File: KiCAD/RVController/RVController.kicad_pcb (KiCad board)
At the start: 2 copper layers, 1 part, among them U1 FREESOC_MINI

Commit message: Getting started
Added GaN NFET output channels, started work on input channels
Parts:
- added C1: 10UF, Capacitor_SMD:C_1206_3216Metric, F.Cu at (114.3, 71.1)
- added J1: 1727078, Footprints:PHOENIX_1727078, F.Cu at (73.7, 66.0)
- added J2: 1727078, Footprints:PHOENIX_1727078, F.Cu at (40.0, 124.5)
- added J3: 1727078, Footprints:PHOENIX_1727078, F.Cu at (40.6, 66.0)
- added J4: 1727078, Footprints:PHOENIX_1727078, F.Cu at (73.7, 124.5)
- added Q1: EPC2014C, Footprints:TRANS_EPC2014C, F.Cu at (92.5, 91.1)
- added Q2: EPC2014C, Footprints:TRANS_EPC2014C, F.Cu at (88.7, 91.1)
- added Q3: EPC2014C, Footprints:TRANS_EPC2014C, F.Cu at (88.7, 88.5)
- added Q4: EPC2014C, Footprints:TRANS_EPC2014C, F.Cu at (92.5, 88.5)
- added Q5: EPC2014C, Footprints:TRANS_EPC2014C, F.Cu at (84.9, 88.5)
- added Q6: EPC2014C, Footprints:TRANS_EPC2014C, F.Cu at (81.0, 91.1)
- added Q7: EPC2014C, Footprints:TRANS_EPC2014C, F.Cu at (76.2, 78.7)
- added Q8: EPC2014C, Footprints:TRANS_EPC2014C, F.Cu at (84.9, 91.1)
- added U2: 74HCT541, Package_DIP:DIP-20_W7.62mm_LongPads, F.Cu at (82.6, 100.3)
- moved U1 62.7 mm to (26.7, 109.2), turned to 90 degrees
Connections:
- U1 pad 20: unconnected-(U1-Pad20) -> GND
- U1 pad 21: unconnected-(U1-Pad21) -> XPWM1
- U1 pad 22: unconnected-(U1-Pad22) -> XPWM2
- U1 pad 23: unconnected-(U1-Pad23) -> XPWM3
- U1 pad 24: unconnected-(U1-Pad24) -> XPWM4
- U1 pad 25: unconnected-(U1-Pad25) -> XPWM5
- U1 pad 26: unconnected-(U1-Pad26) -> XPWM6
- U1 pad 27: unconnected-(U1-Pad27) -> XPWM7
- U1 pad 28: unconnected-(U1-Pad28) -> XPWM8
- U1 pad 40: unconnected-(U1-Pad40) -> +5V

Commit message: Basic layout done
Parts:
- added C2: 100u, Capacitor_THT:CP_Radial_D8.0mm_P3.50mm, F.Cu at (177.5, 95.2)
- added C3: 100u, Capacitor_THT:CP_Radial_D6.3mm_P2.50mm, F.Cu at (147.3, 100.2)
- added C4: 100u, Capacitor_THT:CP_Radial_D6.3mm_P2.50mm, F.Cu at (100.3, 99.7)
- added C5: 100u, Capacitor_THT:CP_Radial_D6.3mm_P2.50mm, F.Cu at (94.7, 93.3)
- added C6: 10UF, Capacitor_SMD:C_1206_3216Metric, F.Cu at (210.8, 83.2)
- added C7: 10UF, Capacitor_SMD:C_1206_3216Metric, F.Cu at (183.5, 94.6)
- added D1: SS16MH, Footprints:SODFL2512X73N, F.Cu at (54.0, 101.6)
- added D10: SS16MH, Footprints:SODFL2512X73N, F.Cu at (90.2, 104.8)
- added D11: SS16MH, Footprints:SODFL2512X73N, F.Cu at (94.0, 101.6)
- added D12: SS16MH, Footprints:SODFL2512X73N, F.Cu at (97.8, 104.8)
- added D13: ATV02W240B, Diode_SMD:D_SOD-123FAC, F.Cu at (38.1, 106.0)
- added D14: ATV02W240B, Footprints:SODFL2512X73N, F.Cu at (109.7, 107.4)
- added D15: ATV02W240B, Diode_SMD:D_SOD-123FAC, F.Cu at (34.9, 106.0)
- added D16: ATV02W240B, Footprints:SODFL2512X73N, F.Cu at (117.0, 107.4)
- added D17: SS16MH, Footprints:SODFL2512X73N, F.Cu at (42.5, 101.0)
- added D18: SS16MH, Footprints:SODFL2512X73N, F.Cu at (42.5, 102.9)
- added D19: SS16MH, Footprints:SODFL2512X73N, F.Cu at (50.2, 101.0)
- added D2: SS16MH, Footprints:SODFL2512X73N, F.Cu at (57.8, 104.8)
- added D20: SS16MH, Footprints:SODFL2512X73N, F.Cu at (50.2, 102.9)
- added D21: ATV02W240B, Footprints:SODFL2512X73N, F.Cu at (124.2, 107.4)
- added D22: ATV02W240B, Footprints:SODFL2512X73N, F.Cu at (131.5, 107.4)
- added D23: ATV02W240B, Footprints:SODFL2512X73N, F.Cu at (141.7, 107.4)
- added D24: ATV02W240B, Footprints:SODFL2512X73N, F.Cu at (148.9, 107.4)
- added D25: ATV02W240B, Footprints:SODFL2512X73N, F.Cu at (156.2, 107.4)
- added D26: ATV02W240B, Footprints:SODFL2512X73N, F.Cu at (163.5, 107.4)
- added D3: SS16MH, Footprints:SODFL2512X73N, F.Cu at (61.6, 101.6)
- added D4: SS16MH, Footprints:SODFL2512X73N, F.Cu at (65.4, 104.8)
- added D5: SS16MH, Footprints:SODFL2512X73N, F.Cu at (71.1, 101.6)
- added D6: SS16MH, Footprints:SODFL2512X73N, F.Cu at (74.9, 104.8)
- added D7: SS16MH, Footprints:SODFL2512X73N, F.Cu at (78.7, 101.6)
- added D8: SS16MH, Footprints:SODFL2512X73N, F.Cu at (82.5, 104.8)
- added D9: SS16MH, Footprints:SODFL2512X73N, F.Cu at (86.4, 101.6)
- added IC1: MCP2561FD-E/P, Package_DIP:DIP-8_W7.62mm_LongPads, F.Cu at (214.6, 87.0)
- added J5: 4-1437652-0, Footprints:TE_4-1437652-0, F.Cu at (174.6, 105.5)
- added J6: Conn_01x02_Male, Connector_PinHeader_2.54mm:PinHeader_1x02_P2.54mm_Vertical, F.Cu at (87.0, 89.5)
- added J7: Conn_01x02_Male, Connector_PinHeader_2.54mm:PinHeader_1x02_P2.54mm_Vertical, F.Cu at (87.0, 93.3)
- added J8: 54602-908LF, Footprints:AMPHENOL_54602-908LF, F.Cu at (217.8, 111.1)
- added J9: 54602-908LF, Footprints:AMPHENOL_54602-908LF, F.Cu at (200.0, 111.1)
- added R1: 1K, Resistor_SMD:R_0805_2012Metric, F.Cu at (56.5, 108.0)
- added R10: 1K, Resistor_SMD:R_0805_2012Metric, F.Cu at (67.9, 108.0)
- added R11: 1K, Resistor_SMD:R_0805_2012Metric, F.Cu at (81.3, 108.0)
- added R12: 1K, Resistor_SMD:R_0805_2012Metric, F.Cu at (88.9, 108.0)
- added R13: 1K, Resistor_SMD:R_0805_2012Metric, F.Cu at (96.5, 108.0)
- added R14: 22K, Resistor_SMD:R_0805_2012Metric, F.Cu at (81.3, 101.6)
- added R15: 22K, Resistor_SMD:R_0805_2012Metric, F.Cu at (88.9, 101.6)
- added R16: 22K, Resistor_SMD:R_0805_2012Metric, F.Cu at (96.5, 101.6)
- added R17: 330R, Resistor_SMD:R_0805_2012Metric, F.Cu at (182.2, 81.9)
- added R18: 1K, Resistor_SMD:R_0805_2012Metric, F.Cu at (77.5, 108.0)
- added R19: 1K, Resistor_SMD:R_0805_2012Metric, F.Cu at (85.1, 108.0)
- added R2: 1K, Resistor_SMD:R_0805_2012Metric, F.Cu at (64.1, 108.0)
- added R20: 1K, Resistor_SMD:R_0805_2012Metric, F.Cu at (92.7, 108.0)
- added R21: 1K, Resistor_SMD:R_0805_2012Metric, F.Cu at (100.3, 108.0)
- added R22: 330R, Resistor_SMD:R_0805_2012Metric, F.Cu at (199.7, 95.9)
- added R25: 4.7K, Resistor_SMD:R_0805_2012Metric, F.Cu at (41.3, 108.0)
- added R26: 1K, Resistor_SMD:R_0805_2012Metric, F.Cu at (42.5, 104.8)
- added R27: 4.7K, Resistor_SMD:R_0805_2012Metric, F.Cu at (48.9, 108.0)
- added R28: 1K, Resistor_SMD:R_0805_2012Metric, F.Cu at (50.2, 104.8)
- added R3: 1K, Resistor_SMD:R_0805_2012Metric, F.Cu at (73.7, 108.0)
- added R4: 22K, Resistor_SMD:R_0805_2012Metric, F.Cu at (56.5, 101.6)
- added R5: 22K, Resistor_SMD:R_0805_2012Metric, F.Cu at (64.1, 101.6)
- added R6: 22K, Resistor_SMD:R_0805_2012Metric, F.Cu at (73.7, 101.6)
- added R7: 1K, Resistor_SMD:R_0805_2012Metric, F.Cu at (45.1, 108.0)
- added R8: 1K, Resistor_SMD:R_0805_2012Metric, F.Cu at (52.7, 108.0)
- added R9: 1K, Resistor_SMD:R_0805_2012Metric, F.Cu at (60.3, 108.0)
- added U3: VX7805-500, Footprints:VX78012-500_VX7805-500, F.Cu at (111.1, 98.4)
- added U4: H11L1SR2M, Footprints:IC_H11L1SR2M, F.Cu at (191.1, 84.5)
- added U5: H11L1SR2M, Footprints:IC_H11L1SR2M, F.Cu at (191.1, 93.3)
- added Y1: ECS-3961-240-AU-TR, Footprints:OSC_ECS-3961-240-AU-TR, F.Cu at (34.4, 99.4)
- moved J3 121.4 mm to (151.8, 114.9), turned to 0 degrees
- moved Q7 88.9 mm to (159.8, 109.2), turned to 180 degrees
- moved C1 84.8 mm to (30.0, 80.1), turned to -90 degrees
- moved Q8 84.1 mm to (167.0, 109.2), turned to 180 degrees
- moved Q6 73.7 mm to (152.5, 109.2), turned to 180 degrees
- moved J1 66.9 mm to (119.4, 114.9), turned to 0 degrees
- moved Q5 63.8 mm to (145.2, 109.2), turned to 180 degrees
- moved U2 58.7 mm to (141.0, 94.6), turned to -90 degrees
- moved Q4 47.3 mm to (135.0, 109.2), turned to 180 degrees
- moved Q3 44.2 mm to (127.8, 109.2), turned to 180 degrees
- moved Q2 36.6 mm to (120.5, 109.2), turned to 180 degrees
- moved Q1 27.5 mm to (113.3, 109.2), turned to 180 degrees
- moved J2 17.4 mm to (54.6, 114.9)
- moved U1 16.8 mm to (33.7, 94.0)
- moved J4 16.4 mm to (87.0, 114.9)
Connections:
- J2 pad 2: GND -> Net-(J2-Pad2)
- J2 pad 4: GND -> Net-(J2-Pad4)
- J2 pad 6: GND -> Net-(J2-Pad6)
- J2 pad 8: GND -> Net-(J2-Pad8)
- J4 pad 2: GND -> Net-(J4-Pad2)
- J4 pad 4: GND -> Net-(J4-Pad4)
- J4 pad 6: GND -> Net-(J4-Pad6)
- J4 pad 8: GND -> Net-(J4-Pad8)
- U1 pad 1: unconnected-(U1-Pad1) -> /CLK_IN
- U1 pad 10: unconnected-(U1-Pad10) -> ADC1
- U1 pad 11: unconnected-(U1-Pad11) -> ADC2
- U1 pad 12: unconnected-(U1-Pad12) -> BUTTON3
- U1 pad 13: unconnected-(U1-Pad13) -> BUTTON4
- U1 pad 14: unconnected-(U1-Pad14) -> BUTTON5
- U1 pad 15: unconnected-(U1-Pad15) -> BUTTON6
- U1 pad 16: unconnected-(U1-Pad16) -> BUTTON7
- U1 pad 17: unconnected-(U1-Pad17) -> BUTTON8
- U1 pad 21: XPWM1 -> XPWM8
- U1 pad 22: XPWM2 -> XPWM7
- U1 pad 23: XPWM3 -> XPWM6
- U1 pad 24: XPWM4 -> XPWM5
- U1 pad 25: XPWM5 -> XPWM4
- U1 pad 26: XPWM6 -> XPWM3
- U1 pad 27: XPWM7 -> XPWM2
- U1 pad 28: XPWM8 -> XPWM1
- U2 pad 11: PWM8 -> PWM1
- U2 pad 12: PWM7 -> PWM2
- U2 pad 13: PWM6 -> PWM3
- U2 pad 14: PWM5 -> PWM4
- U2 pad 15: PWM4 -> PWM5
- U2 pad 16: PWM3 -> PWM6
- U2 pad 17: PWM2 -> PWM7
- U2 pad 18: PWM1 -> PWM8
- U2 pad 2: XPWM1 -> XPWM8
- U2 pad 3: XPWM2 -> XPWM7
- U2 pad 4: XPWM3 -> XPWM6
- U2 pad 5: XPWM4 -> XPWM5
- U2 pad 6: XPWM5 -> XPWM4
- U2 pad 7: XPWM6 -> XPWM3
- U2 pad 8: XPWM7 -> XPWM2
- U2 pad 9: XPWM8 -> XPWM1
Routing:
- net +5V: track 0.00 -> 277.7 mm, vias 0 -> 9
- net GNDPWR: track 0.00 -> 86.7 mm
- net GND: track 0.00 -> 77.6 mm, vias 0 -> 36
- net XPWM2: track 0.00 -> 67.8 mm
- net XPWM3: track 0.00 -> 67.8 mm
- net XPWM4: track 0.00 -> 67.8 mm
- net XPWM6: track 0.00 -> 67.4 mm
- net XPWM5: track 0.00 -> 67.4 mm
- net XPWM1: track 0.00 -> 67.1 mm
- net XPWM8: track 0.00 -> 66.8 mm
- net XPWM7: track 0.00 -> 66.6 mm
- net ADC1: track 0.00 -> 59.4 mm
- net +5V_CAN: track 0.00 -> 58.8 mm, vias 0 -> 1
- net ADC2: track 0.00 -> 51.6 mm
- net CANH: track 0.00 -> 36.9 mm
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- added copper zone on B.Cu, net GND
- added copper zone on F.Cu, net GND
- added copper zone on F.Cu, net LED1
- added copper zone on F.Cu, net LED2
- added copper zone on F.Cu, net LED3
- added copper zone on F.Cu, net LED4
- added copper zone on F.Cu, net LED5
- added copper zone on F.Cu, net LED6
- added copper zone on F.Cu, net LED7
- added copper zone on F.Cu, net LED8
- added copper zone on B.Cu, net VBUS
- added copper zone on F.Cu, net VBUS
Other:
- board outline added: 210.8 x 59.7 mm

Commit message: Almost done
Added mounting holes, labels, etc.
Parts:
- added H1: MountingHole, MountingHole:MountingHole_3.2mm_M3_ISO14580, F.Cu at (106.3, 121.4)
- added H2: MountingHole, MountingHole:MountingHole_3.2mm_M3_ISO14580, F.Cu at (201.2, 121.7)
- added H3: MountingHole, MountingHole:MountingHole_3.2mm_M3_ISO14580, F.Cu at (242.4, 121.3)
- added H4: MountingHole, MountingHole:MountingHole_3.2mm_M3_ISO14580, F.Cu at (242.6, 77.3)
- added H5: MountingHole, MountingHole:MountingHole_3.2mm_M3_ISO14580, F.Cu at (135.5, 77.5)
- added H6: MountingHole, MountingHole:MountingHole_3.2mm_M3_ISO14580, F.Cu at (24.0, 77.5)
- added H7: MountingHole, MountingHole:MountingHole_3.2mm_M3_ISO14580, F.Cu at (24.0, 121.4)
- moved J8 14.4 mm to (230.6, 117.6)
- moved J9 14.4 mm to (212.9, 117.6)
- moved U4 12.9 mm to (204.0, 84.2)
- moved C6 12.9 mm to (223.7, 83.2)
- moved IC1 12.9 mm to (227.5, 87.0)
- moved R17 12.9 mm to (195.1, 81.9)
- moved R22 12.9 mm to (212.6, 95.9)
- moved U5 12.9 mm to (204.0, 93.3)
- moved C7 11.8 mm to (195.4, 94.5)
- moved J5 7.52 mm to (182.1, 105.5)
- moved C2 7.52 mm to (185.0, 95.9)
- moved J3 6.35 mm to (158.1, 114.9)
- moved Q8 6.35 mm to (173.4, 109.2)
- moved D14 6.35 mm to (116.1, 107.4)
- moved J1 6.35 mm to (125.7, 114.9)
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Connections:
- U1 pad 29: unconnected-(U1-Pad29) -> /CAN_RX
- U1 pad 30: unconnected-(U1-Pad30) -> /CAN_TX
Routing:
- net /CAN_RX: track 0.00 -> 145.5 mm
- net /CAN_TX: track 0.00 -> 144.0 mm
- net GNDPWR: track 86.7 -> 7.80 mm, vias 0 -> 2
- net +5V: track 277.7 -> 338.4 mm, vias 9 -> 11
- net VBUS: track 26.2 -> 75.5 mm, vias 0 -> 2
- net PWM8: track 0.00 -> 42.4 mm
- net PWM7: track 0.00 -> 36.5 mm
- net PWM6: track 0.00 -> 32.2 mm
- net PWM5: track 0.00 -> 27.5 mm
- net PWM4: track 0.00 -> 19.3 mm
- net PWM3: track 0.00 -> 15.3 mm
- net XPWM8: track 66.8 -> 82.2 mm
- net +5V_CAN: track 58.8 -> 71.1 mm
- net PWM1: track 0.00 -> 12.0 mm
- net PWM2: track 0.00 -> 9.96 mm
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- added copper zone on B.Cu, net GNDPWR
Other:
- board size 210.8 x 59.7 mm -> 227.2 x 53 mm
- board text added: "1 CANH"
- board text added: "12V 24V"
- board text added: "2 CANL"
- board text added: "3 GND"
- board text added: "4 NC"
- board text added: "5 NC"
- board text added: "6 NC"
- board text added: "7 GND"
- board text added: "8 +5V"
- board text added: "ADC1"
- board text added: "ADC2"
- board text added: "B1+"
- board text added: "B1-"
- board text added: "B2+"
- board text added: "B2-"
- board text added: "B3+"
- board text added: "B3-"
- board text added: "B4+"
- board text added: "B4-"
- board text added: "B5+"
- board text added: "B5-"
- board text added: "B6+"
- board text added: "B6-"
- board text added: "GND"
- board text added: "Isolated CANbus"
- board text added: "LED1"
- board text added: "LED2"
- board text added: "LED3"
- board text added: "LED4"
- board text added: "LED5"
- board text added: "LED6"
- board text added: "LED7"
- board text added: "LED8"
- board text added: "V+"

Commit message: Done?
Routed, etc. Exported STEP.
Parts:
- added C8: 4700pF, Capacitor_SMD:C_0603_1608Metric, F.Cu at (238.2, 98.7)
- added J10: Conn_01x02_Male, Connector_PinHeader_2.54mm:PinHeader_1x02_P2.54mm_Vertical, F.Cu at (231.5, 96.3)
- added J11: Conn_01x02_Male, Connector_PinHeader_2.54mm:PinHeader_1x02_P2.54mm_Vertical, F.Cu at (231.5, 92.6)
- added J12: 284392-2, Footprints:TE_284392-2, F.Cu at (242.7, 106.7)
- added R23: 300R, Resistor_SMD:R_0805_2012Metric, F.Cu at (219.7, 98.4)
- added R24: 60R, Resistor_SMD:R_0805_2012Metric, F.Cu at (238.0, 96.3)
- added R29: 60R, Resistor_SMD:R_0805_2012Metric, F.Cu at (238.0, 92.6)
- R17, R22: value 330R -> 300R
- renumbered Q5 to locked, Q4 to locked, Q7 to locked, Q2 to locked, Q8 to locked, Q6 to locked, Q1 to locked, Q3 to locked
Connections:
- net GNDPWR renamed GND_CAN
- IC1 pad 5: unconnected-(IC1-Pad5) -> Net-(IC1-Pad5)
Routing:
- net Net-(C8-Pad1): track 0.00 -> 38.5 mm
- net +5V_CAN: track 71.1 -> 85.6 mm
- net CANL: track 42.7 -> 53.5 mm
- net CANH: track 37.5 -> 44.5 mm
- net Net-(J11-Pad2): track 0.00 -> 3.03 mm
- net Net-(J10-Pad2): track 0.00 -> 3.03 mm
- net Net-(IC1-Pad5): track 0.00 -> 3.00 mm
- net GND_CAN: track 7.80 -> 9.82 mm, vias 2 -> 3
- net Net-(IC1-Pad4): track 14.5 -> 13.7 mm
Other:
- board text added: "5V_CAN"
- board text added: "Close Jumpers to Terminate"
- board text added: "GND_CAN"

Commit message: Updated to SMD socket
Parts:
- C3: value 100u -> C
- D14, D16, D21, D22, D23, D24, D25, D26: value ATV02W240B -> SS16MH; footprint Footprints:SODFL2512X73N -> Diode_SMD:D_SOD-123FAC
- moved C2 1.52 mm to (185.0, 94.4)
- moved D14 1.39 mm to (116.8, 108.6), turned to 90 degrees
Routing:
- net PWM5: track 27.5 -> 32.4 mm
- net LED7: track 7.79 -> 2.91 mm
- net LED6: track 7.19 -> 2.31 mm
- net PWM6: track 32.2 -> 37.1 mm
- net VBUS: track 75.5 -> 74.4 mm

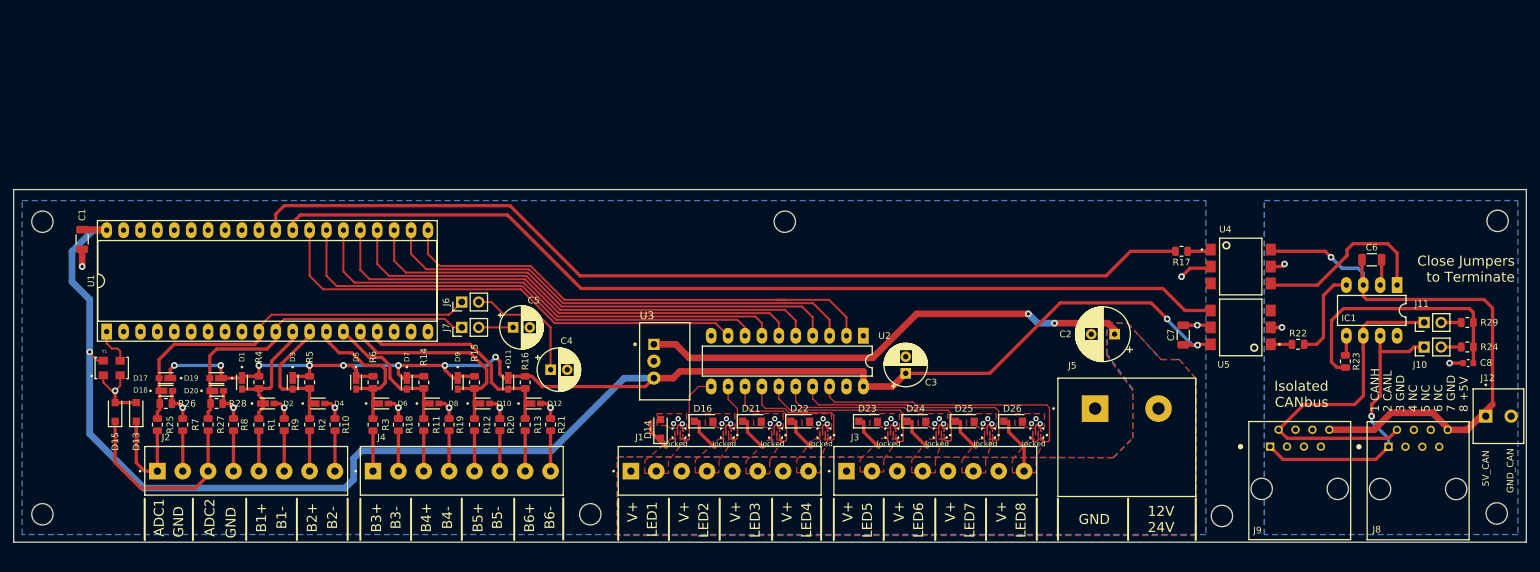
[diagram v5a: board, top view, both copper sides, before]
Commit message: Updates to new parts, routed
Changed to alternative FETs, Schottky diodes, TVS, etc. Ready for production
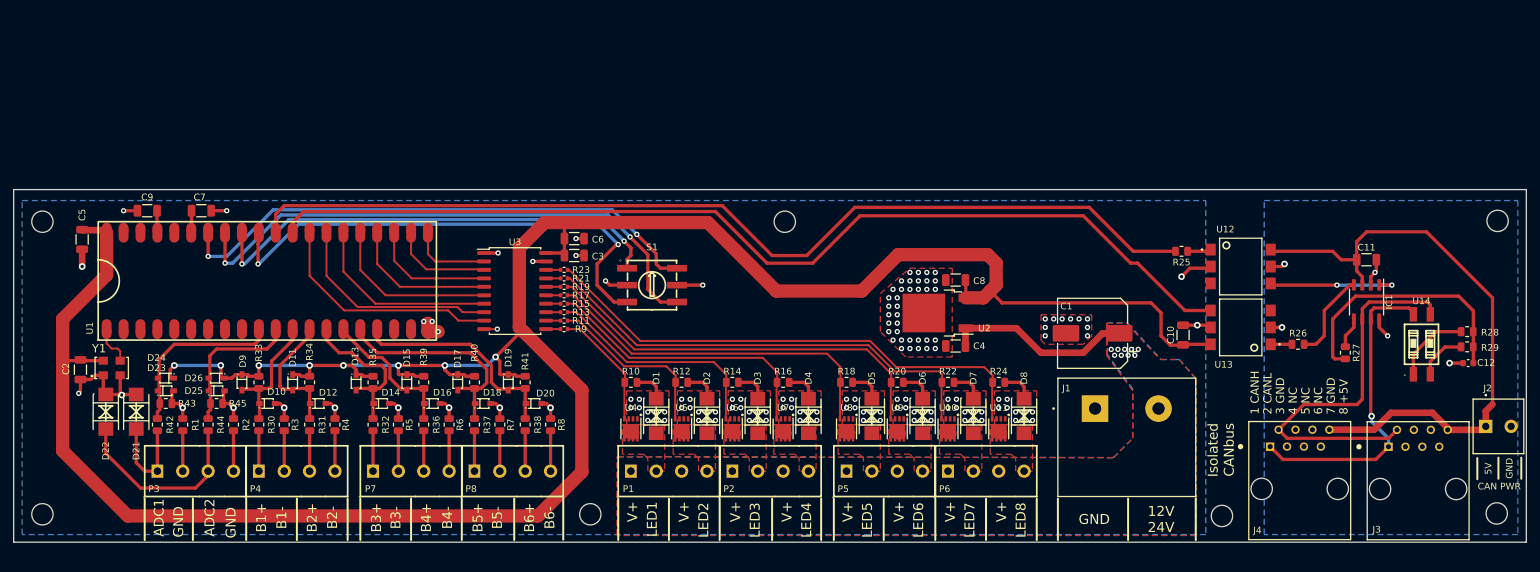
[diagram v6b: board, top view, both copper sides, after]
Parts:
- removed the C4 at (100.3, 99.7)
- removed the C5 at (94.7, 93.3)
- removed the J1 at (125.7, 114.9)
- removed J10, J11, J6, J7: Conn_01x02_Male, Connector_PinHeader_2.54mm:PinHeader_1x02_P2.54mm_Vertical
- removed the J2 at (54.6, 114.9)
- removed the J3 at (158.1, 114.9)
- removed the J4 at (87.0, 114.9)
- removed locked (x8): EPC2014C, Footprints:TRANS_EPC2014C
- added C2: 1206,100nF,50V,X7R, Capacitor_SMD:C_1206_3216Metric, F.Cu at (29.7, 99.7)
- added C3: 1206,100nF,50V,X7R, Capacitor_SMD:C_1206_3216Metric, F.Cu at (103.9, 82.5)
- added C6: 10UF, Capacitor_SMD:C_1206_3216Metric, F.Cu at (103.9, 80.0)
- added C7: 1206,1uF,50V,X7R, Capacitor_SMD:C_1206_3216Metric, F.Cu at (47.9, 75.8)
- added C8: 1206,100nF,50V,X7R, Capacitor_SMD:C_1206_3216Metric, F.Cu at (161.2, 86.2)
- added C9: 1206,1uF,50V,X7R, Capacitor_SMD:C_1206_3216Metric, F.Cu at (39.8, 75.8)
- added P1: WJ124-3_81-4P, Footprints:CONN-TH_4P-P3.81_KF124-3.81-4P, F.Cu at (118.1, 114.9)
- added P2: WJ124-3_81-4P, Footprints:CONN-TH_4P-P3.81_KF124-3.81-4P, F.Cu at (133.3, 114.9)
- added P3: WJ124-3_81-4P, Footprints:CONN-TH_4P-P3.81_KF124-3.81-4P, F.Cu at (47.0, 114.9)
- added P4: WJ124-3_81-4P, Footprints:CONN-TH_4P-P3.81_KF124-3.81-4P, F.Cu at (62.2, 114.9)
- added P5: WJ124-3_81-4P, Footprints:CONN-TH_4P-P3.81_KF124-3.81-4P, F.Cu at (150.5, 114.9)
- added P6: WJ124-3_81-4P, Footprints:CONN-TH_4P-P3.81_KF124-3.81-4P, F.Cu at (165.7, 114.9)
- added P7: WJ124-3_81-4P, Footprints:CONN-TH_4P-P3.81_KF124-3.81-4P, F.Cu at (79.4, 114.9)
- added P8: WJ124-3_81-4P, Footprints:CONN-TH_4P-P3.81_KF124-3.81-4P, F.Cu at (94.6, 114.9)
- added R10: 1K, Resistor_SMD:R_0805_2012Metric, F.Cu at (112.4, 101.6)
- added R11: 0402,47, Resistor_SMD:R_0402_1005Metric, F.Cu at (102.4, 92.3)
- added R12: 1K, Resistor_SMD:R_0805_2012Metric, F.Cu at (120.0, 101.6)
- added R13: 0402,47, Resistor_SMD:R_0402_1005Metric, F.Cu at (102.4, 91.1)
- added R14: 1K, Resistor_SMD:R_0805_2012Metric, F.Cu at (127.6, 101.6)
- added R15: 0402,47, Resistor_SMD:R_0402_1005Metric, F.Cu at (102.4, 89.8)
- added R16: 1K, Resistor_SMD:R_0805_2012Metric, F.Cu at (135.3, 101.6)
- added R17: 0402,47, Resistor_SMD:R_0402_1005Metric, F.Cu at (102.4, 88.5)
- added R18: 1K, Resistor_SMD:R_0805_2012Metric, F.Cu at (144.8, 101.6)
- added R19: 0402,47, Resistor_SMD:R_0402_1005Metric, F.Cu at (102.4, 87.2)
- added R20: 1K, Resistor_SMD:R_0805_2012Metric, F.Cu at (152.4, 101.6)
- added R21: 0402,47, Resistor_SMD:R_0402_1005Metric, F.Cu at (102.4, 86.0)
- added R22: 1K, Resistor_SMD:R_0805_2012Metric, F.Cu at (160.0, 101.6)
- added R23: 0402,47, Resistor_SMD:R_0402_1005Metric, F.Cu at (102.4, 84.7)
- added R24: 1K, Resistor_SMD:R_0805_2012Metric, F.Cu at (167.6, 101.6)
- added R9: 0402,47, Resistor_SMD:R_0402_1005Metric, F.Cu at (102.4, 93.6)
- added S1: MSDR-16S, Footprints:SW-SMD_6P-L7.4-W7.4-P2.54-LS9.5-TL, F.Cu at (115.6, 87.0)
- added U10: AON7410, Footprints:DFN-8_L3.0-W3.0-P0.65-BL, F.Cu at (160.0, 108.6)
- added U11: AON7410, Footprints:DFN-8_L3.0-W3.0-P0.65-BL, F.Cu at (167.6, 108.6)
- added U14: DSIC02LSGET, Footprints:SW-SMD_4P-L6.0-W5.1-P2.54-LS9.3-BL, F.Cu at (231.1, 95.9)
- added U4: AON7410, Footprints:DFN-8_L3.0-W3.0-P0.65-BL, F.Cu at (112.4, 108.6)
- added U5: AON7410, Footprints:DFN-8_L3.0-W3.0-P0.65-BL, F.Cu at (120.0, 108.6)
- added U6: AON7410, Footprints:DFN-8_L3.0-W3.0-P0.65-BL, F.Cu at (127.6, 108.6)
- added U7: AON7410, Footprints:DFN-8_L3.0-W3.0-P0.65-BL, F.Cu at (135.3, 108.6)
- added U8: AON7410, Footprints:DFN-8_L3.0-W3.0-P0.65-BL, F.Cu at (144.8, 108.6)
- added U9: AON7410, Footprints:DFN-8_L3.0-W3.0-P0.65-BL, F.Cu at (152.4, 108.6)
- C1: renamed from C2; value 100u -> HZA107M050G24T-F; footprint Capacitor_THT:CP_Radial_D8.0mm_P3.50mm -> Capacitor_SMD:CP_Elec_10x10
- C4: renamed from C3; value C -> 1206,100nF,50V,X7R; footprint Capacitor_THT:CP_Radial_D6.3mm_P2.50mm -> Capacitor_SMD:C_1206_3216Metric
- D1: renamed from D14; value SS16MH -> SMBJ15CA-C78410; footprint Diode_SMD:D_SOD-123FAC -> Footprints:SMB_L4.6-W3.6-LS5.3-BI
- D10: renamed from D2; footprint Footprints:SODFL2512X73N -> Footprints:SOD-323_L1.8-W1.3-LS2.5-RD
- D11: renamed from D3; footprint Footprints:SODFL2512X73N -> Footprints:SOD-323_L1.8-W1.3-LS2.5-RD
- D12: renamed from D4; footprint Footprints:SODFL2512X73N -> Footprints:SOD-323_L1.8-W1.3-LS2.5-RD
- D13: renamed from D5; footprint Footprints:SODFL2512X73N -> Footprints:SOD-323_L1.8-W1.3-LS2.5-RD
- D14: renamed from D6; footprint Footprints:SODFL2512X73N -> Footprints:SOD-323_L1.8-W1.3-LS2.5-RD
- D15: renamed from D7; footprint Footprints:SODFL2512X73N -> Footprints:SOD-323_L1.8-W1.3-LS2.5-RD
- D16: renamed from D8; footprint Footprints:SODFL2512X73N -> Footprints:SOD-323_L1.8-W1.3-LS2.5-RD
- D17: renamed from D9; footprint Footprints:SODFL2512X73N -> Footprints:SOD-323_L1.8-W1.3-LS2.5-RD
- D18: renamed from D10; footprint Footprints:SODFL2512X73N -> Footprints:SOD-323_L1.8-W1.3-LS2.5-RD
- D19: renamed from D11; footprint Footprints:SODFL2512X73N -> Footprints:SOD-323_L1.8-W1.3-LS2.5-RD
- D2: renamed from D16; value SS16MH -> SMBJ15CA-C78410; footprint Diode_SMD:D_SOD-123FAC -> Footprints:SMB_L4.6-W3.6-LS5.3-BI
- D20: renamed from D12; footprint Footprints:SODFL2512X73N -> Footprints:SOD-323_L1.8-W1.3-LS2.5-RD
- D21: renamed from D13; value ATV02W240B -> SMBJ15CA-C78410; footprint Diode_SMD:D_SOD-123FAC -> Footprints:SMB_L4.6-W3.6-LS5.3-BI
- D22: renamed from D15; value ATV02W240B -> SMBJ15CA-C78410; footprint Diode_SMD:D_SOD-123FAC -> Footprints:SMB_L4.6-W3.6-LS5.3-BI
- D23: renamed from D17; footprint Footprints:SODFL2512X73N -> Footprints:SOD-323_L1.8-W1.3-LS2.5-RD
- D24: renamed from D18; footprint Footprints:SODFL2512X73N -> Footprints:SOD-323_L1.8-W1.3-LS2.5-RD
- D25: renamed from D19; footprint Footprints:SODFL2512X73N -> Footprints:SOD-323_L1.8-W1.3-LS2.5-RD
- D26: renamed from D20; footprint Footprints:SODFL2512X73N -> Footprints:SOD-323_L1.8-W1.3-LS2.5-RD
- D3: renamed from D21; value SS16MH -> SMBJ15CA-C78410; footprint Diode_SMD:D_SOD-123FAC -> Footprints:SMB_L4.6-W3.6-LS5.3-BI
- D4: renamed from D22; value SS16MH -> SMBJ15CA-C78410; footprint Diode_SMD:D_SOD-123FAC -> Footprints:SMB_L4.6-W3.6-LS5.3-BI
- D5: renamed from D23; value SS16MH -> SMBJ15CA-C78410; footprint Diode_SMD:D_SOD-123FAC -> Footprints:SMB_L4.6-W3.6-LS5.3-BI
- D6: renamed from D24; value SS16MH -> SMBJ15CA-C78410; footprint Diode_SMD:D_SOD-123FAC -> Footprints:SMB_L4.6-W3.6-LS5.3-BI
- D7: renamed from D25; value SS16MH -> SMBJ15CA-C78410; footprint Diode_SMD:D_SOD-123FAC -> Footprints:SMB_L4.6-W3.6-LS5.3-BI
- D8: renamed from D26; value SS16MH -> SMBJ15CA-C78410; footprint Diode_SMD:D_SOD-123FAC -> Footprints:SMB_L4.6-W3.6-LS5.3-BI
- D9: renamed from D1; footprint Footprints:SODFL2512X73N -> Footprints:SOD-323_L1.8-W1.3-LS2.5-RD
- IC1: value MCP2561FD-E/P -> TJA1042T/1J; footprint Package_DIP:DIP-8_W7.62mm_LongPads -> Package_SO:SO-8_3.9x4.9mm_P1.27mm
- U1: value FREESOC_MINI -> 114-83-640-41-134161; footprint Package_DIP:DIP-40_W15.24mm_Socket_LongPads -> Footprints:114-83-640-41-134161
- U2: renamed from U3; value VX7805-500 -> CJ7805_3%; footprint Footprints:VX78012-500_VX7805-500 -> Package_TO_SOT_SMD:TO-252-2
- U3: renamed from U2; value 74HCT541 -> C554416; footprint Package_DIP:DIP-20_W7.62mm_LongPads -> Package_SO:SOIC-20W_7.5x12.8mm_P1.27mm
- moved U3 52.7 mm to (95.0, 87.9), turned to 0 degrees
- moved U2 41.7 mm to (158.5, 91.2), turned to 180 degrees
- moved U1 25.3 mm to (57.8, 86.4)
- moved C4 8.54 mm to (161.2, 96.1), turned to 180 degrees
- moved IC1 5.25 mm to (222.9, 89.5)
- moved R29 3.66 mm to (238.0, 96.3), turned to 0 degrees
- moved C1 3.31 mm to (181.7, 94.2)
- moved R28 2.31 mm to (238.0, 94.0), turned to 180 degrees
- moved D1 2.01 mm to (116.2, 106.7), turned to -90 degrees
- moved D8 1.81 mm to (171.4, 106.7), turned to -90 degrees
- moved J2 1.53 mm to (242.7, 108.2)
- moved D7 1.49 mm to (163.8, 106.7), turned to -90 degrees
- moved D4 1.45 mm to (139.1, 106.7), turned to -90 degrees
- moved D22 1.40 mm to (33.5, 106.0), turned to -90 degrees
- moved R27 1.29 mm to (219.7, 97.2)
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- renumbered C7 to C10, C6 to C11, C8 to C12, C1 to C5, J5 to J1, J12 to J2, J8 to J3, J9 to J4, R7 to R1, R8 to R2, R17 to R25, R22 to R26, R23 to R27, R24 to R28, R9 to R3, R1 to R30, R2 to R31, R3 to R32, R4 to R33, R5 to R34, R6 to R35, R11 to R36, R12 to R37, R13 to R38, R14 to R39, R10 to R4, R15 to R40, R16 to R41, R25 to R42, R26 to R43, R27 to R44, R28 to R45, R18 to R5, R19 to R6, R20 to R7, R21 to R8, U4 to U12, U5 to U13
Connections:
- C12 pad 1: Net-(C8-Pad1) -> Net-(C12-Pad1)
- C4 pad 1: +5V -> VBUS
- R27 pad 2: Net-(C8-Pad1) -> Net-(C12-Pad1)
- R28 pad 1: Net-(J10-Pad2) -> Net-(C12-Pad1)
- R28 pad 2: Net-(C8-Pad1) -> Net-(R28-Pad2)
- R29 pad 1: Net-(C8-Pad1) -> Net-(R29-Pad1)
- R29 pad 2: Net-(J11-Pad2) -> Net-(C12-Pad1)
- U1 pad 31: unconnected-(U1-Pad31) -> /ADDR_4
- U1 pad 32: unconnected-(U1-Pad32) -> /ADDR_1
- U1 pad 33: unconnected-(U1-Pad33) -> /ADDR_2
- U1 pad 34: unconnected-(U1-Pad34) -> /ADDR_8
- U1 pad 35: unconnected-(U1-Pad35) -> Net-(C7-Pad2)
- U1 pad 37: unconnected-(U1-Pad37) -> Net-(C9-Pad2)
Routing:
- net /ADDR_2: track 0.00 -> 82.4 mm, vias 0 -> 2
- net /ADDR_8: track 0.00 -> 81.8 mm, vias 0 -> 2
- net Net-(R23-Pad2): track 0.00 -> 77.0 mm
- net /ADDR_4: track 0.00 -> 74.2 mm, vias 0 -> 2
- net XPWM8: track 82.2 -> 10.6 mm
- net /ADDR_1: track 0.00 -> 71.3 mm, vias 0 -> 2
- net Net-(R21-Pad2): track 0.00 -> 69.0 mm
- net Net-(R19-Pad2): track 0.00 -> 60.8 mm
- net XPWM7: track 72.9 -> 13.6 mm
- net XPWM6: track 73.8 -> 17.3 mm
- net +5V: track 338.4 -> 393.5 mm, vias 11 -> 8
- net Net-(R17-Pad2): track 0.00 -> 53.3 mm
- net XPWM5: track 73.7 -> 20.6 mm
- net GND: track 75.0 -> 126.2 mm, vias 36 -> 151
- net XPWM4: track 74.1 -> 24.2 mm
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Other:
- board text added: "5V"
- board text added: "CAN PWR"
- board text removed: "5V_CAN"
- board text removed: "Close Jumpers to Terminate"
- board text removed: "GND_CAN"
